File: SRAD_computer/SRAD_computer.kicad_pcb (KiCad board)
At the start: 2 copper layers, 80 x 90 mm, 73 parts, among them J1 Terminal_3, J2 Conn_01x02, J4 Terminal_2, J5 Connector_3_Pol, J6 Micro_SD_Card, J7 UJ20-C-H-G-SMT-6-P16-TR, Q1 MMBT5551L, Q3 FDN340P, U1 NCP1117-3.3_SOT223, U2 W25Q128JVS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

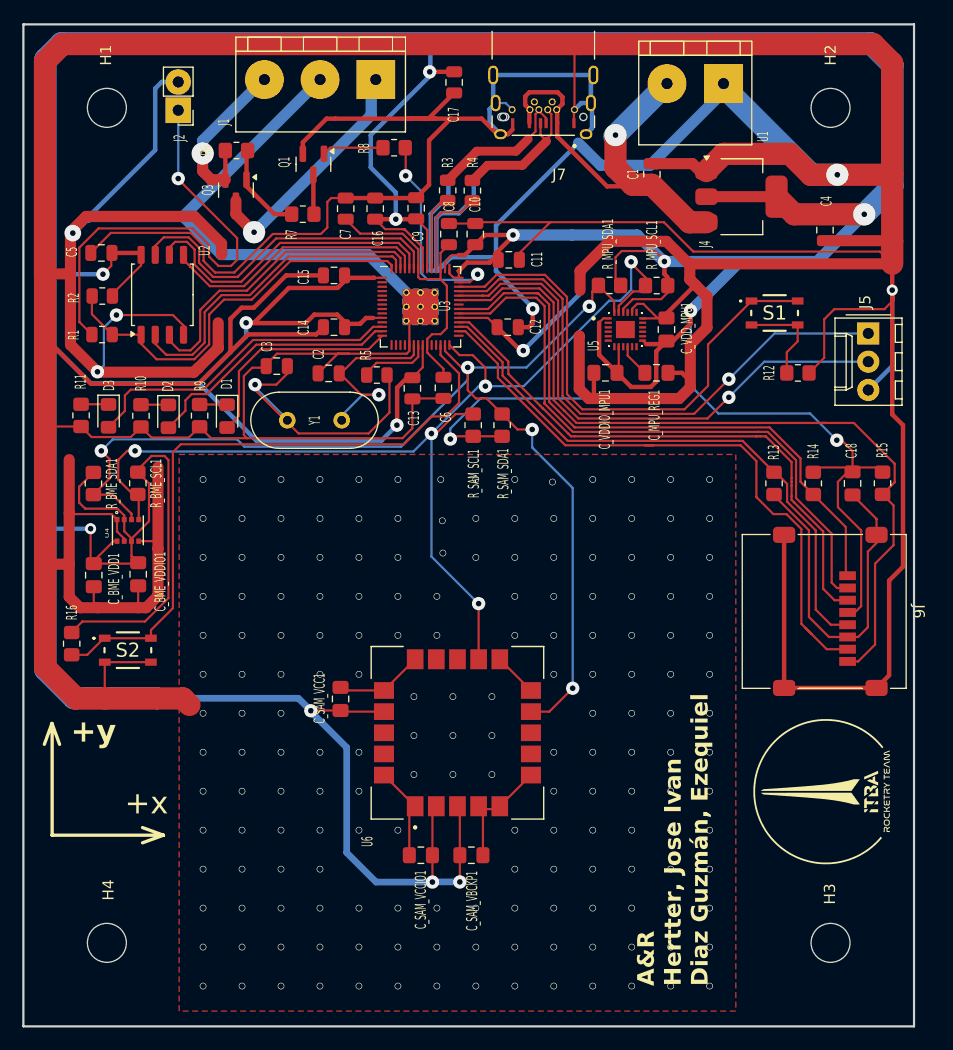
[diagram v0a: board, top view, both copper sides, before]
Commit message: reboot and bootsel buttons added
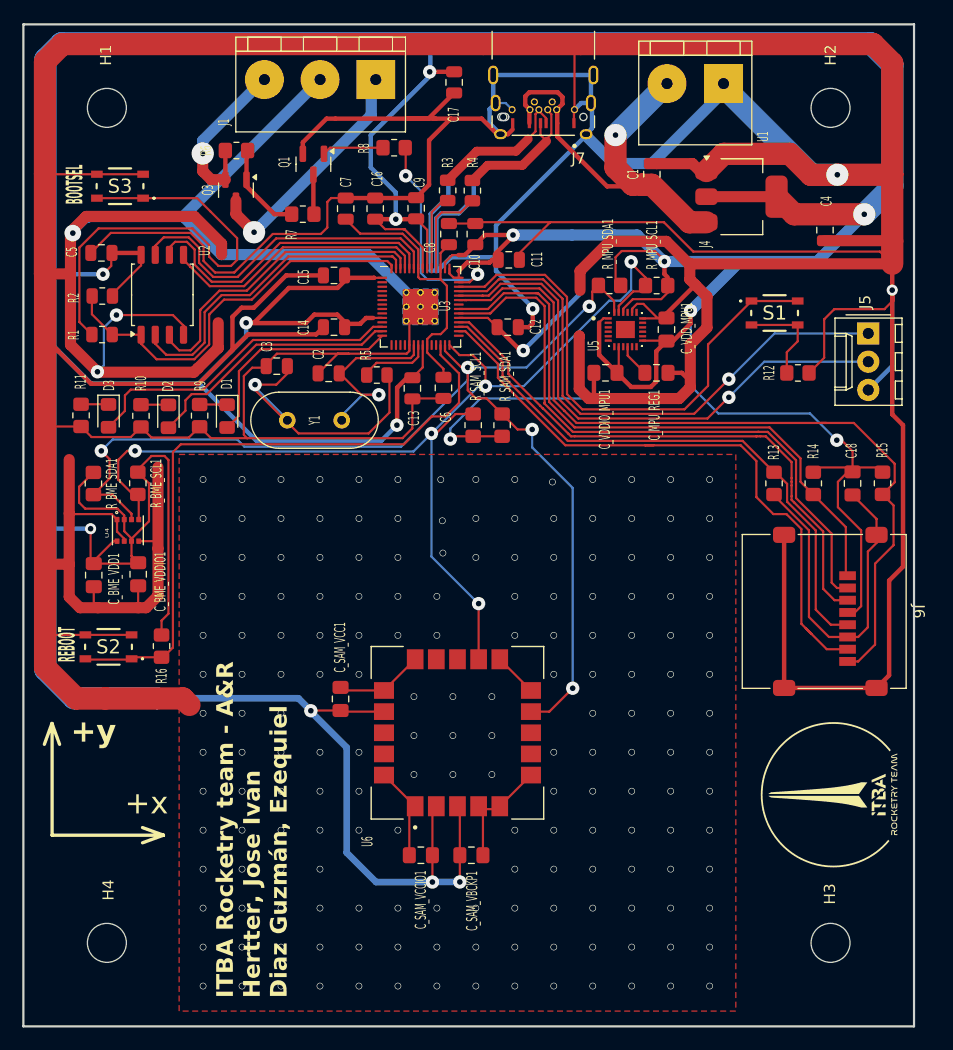
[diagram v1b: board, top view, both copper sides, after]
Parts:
- removed J2: Conn_01x02, Connector_PinHeader_2.54mm:PinHeader_1x02_P2.54mm_Vertical
- added S3: PTS810SJK250SMTR_LFS, Rocketry_FC:PTS810SJK250SMTRLFS, F.Cu at (64.6, 49.9)
- moved R16 8.07 mm to (68.3, 91.2)
- moved S2 1.77 mm to (63.5, 91.2), turned to 180 degrees
- moved G*** 0.73 mm to (128.8, 104.5)
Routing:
- net GND: track 951.9 -> 945.2 mm
- net +3V3: track 617.7 -> 611.1 mm
- net /~{USB_BOOT}: track 41.0 -> 41.4 mm, vias 1 -> 0
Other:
- board text added: "BOOTSEL"
- board text added: "ITBA Rocketry team - A&R Hertter, Jose Ivan Diaz Guzmán, Ezequiel"
- board text added: "REBOOT"
- board text removed: "A&R Hertter, Jose Ivan Diaz Guzmán, Ezequiel"

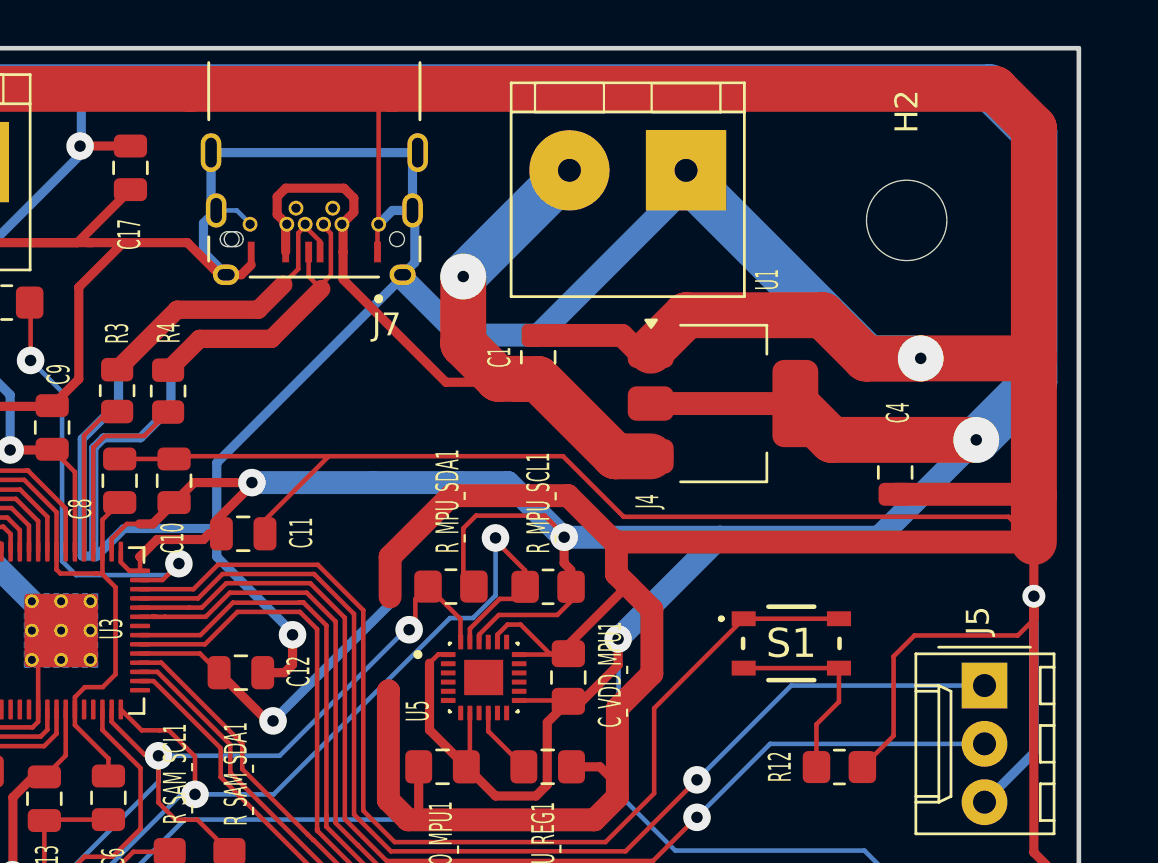
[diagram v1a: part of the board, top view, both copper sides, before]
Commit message: Pin for battery level added
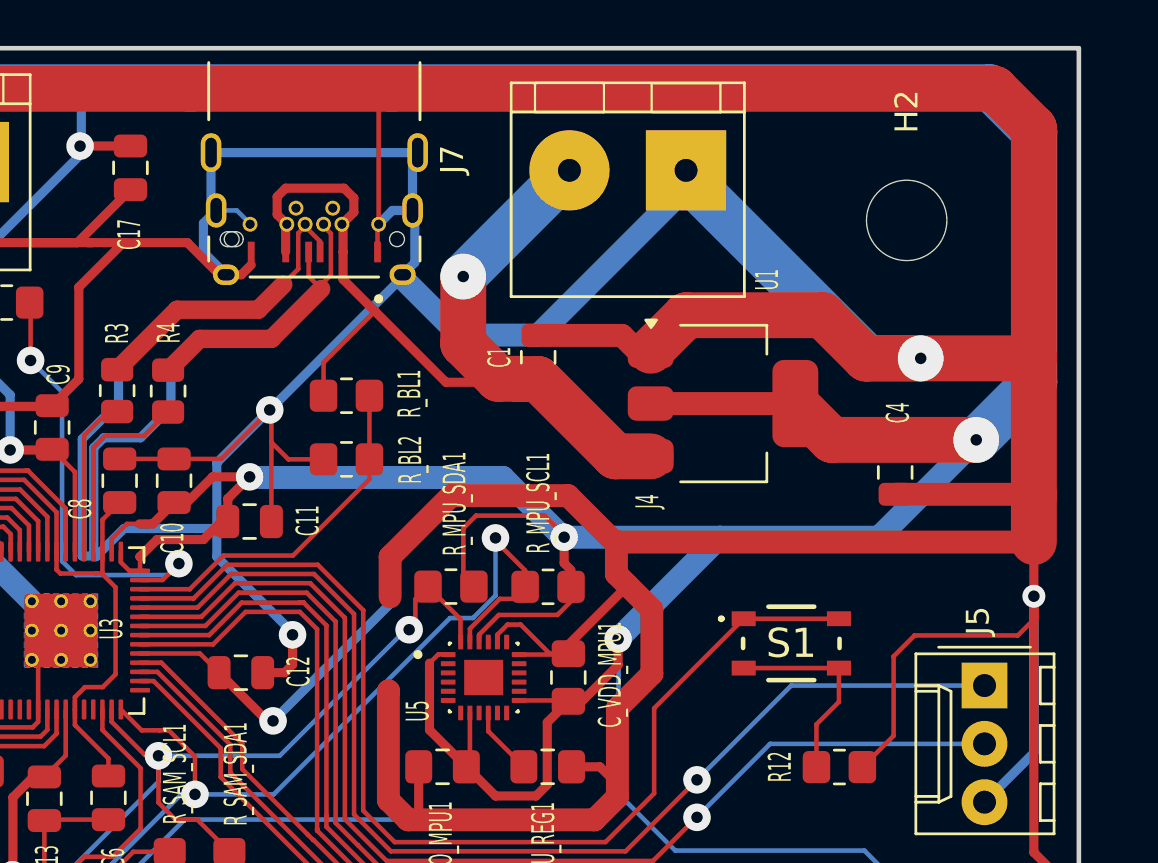
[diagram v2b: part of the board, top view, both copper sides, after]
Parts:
- added R_BL1: R, TCLib:R_0805, F.Cu at (104.0, 50.5)
- added R_BL2: R, TCLib:R_0805, F.Cu at (104.0, 53.2)
- moved C11 0.60 mm to (99.8, 55.9)
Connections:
- U3 pad 36: /GPIO24 -> /SD_DAT1
- U3 pad 37: /SD_DAT1 -> /UART_Tx
- U3 pad 38: /UART_Tx -> /UART_Rx
- U3 pad 39: /UART_Rx -> /SW_1
- U3 pad 40: /SW_1 -> /BAT_LVL
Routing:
- net GND: track 945.2 -> 914.6 mm, vias 184 -> 185
- net /BAT_LVL: track 0.00 -> 15.6 mm
- net VBUS: track 40.1 -> 44.7 mm
- net +3V3: track 611.1 -> 613.8 mm

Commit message: Gerber files added
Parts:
- removed Q1: MMBT5551L, Package_TO_SOT_SMD:SOT-23
- removed Q3: FDN340P, Package_TO_SOT_SMD:SOT-23
- removed R6, R7, R8: R, TCLib:R_0805
- J1: value Terminal_3 -> Connector_2_Pol; footprint TCLib:Bornera_3_P5mm -> TCLib:Molex_1x02_P2.54mm
- moved J1 1.69 mm to (85.8, 40.3), turned to 0 degrees
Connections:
- J1 pad 1: /V_cam -> GND
- J1 pad 2: GND -> /servo
- U3 pad 41: /power_cam -> /servo
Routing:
- net /servo: track 0.00 -> 26.5 mm, vias 0 -> 1
- net /V_cam: track 21.8 -> 0.00 mm, vias 1 -> 0
- net /power_cam: track 19.4 -> 0.00 mm, vias 2 -> 0
- net V_cam_bus: track 15.5 -> 0.00 mm, vias 1 -> 0
- net GND: track 914.6 -> 899.6 mm
- net Net-(Q3-G): track 8.35 -> 0.00 mm
- net Net-(Q1-B): track 5.53 -> 0.00 mm
- net Net-(Q1-C): track 3.57 -> 0.00 mm
- net +3V3: track 613.8 -> 611.9 mm

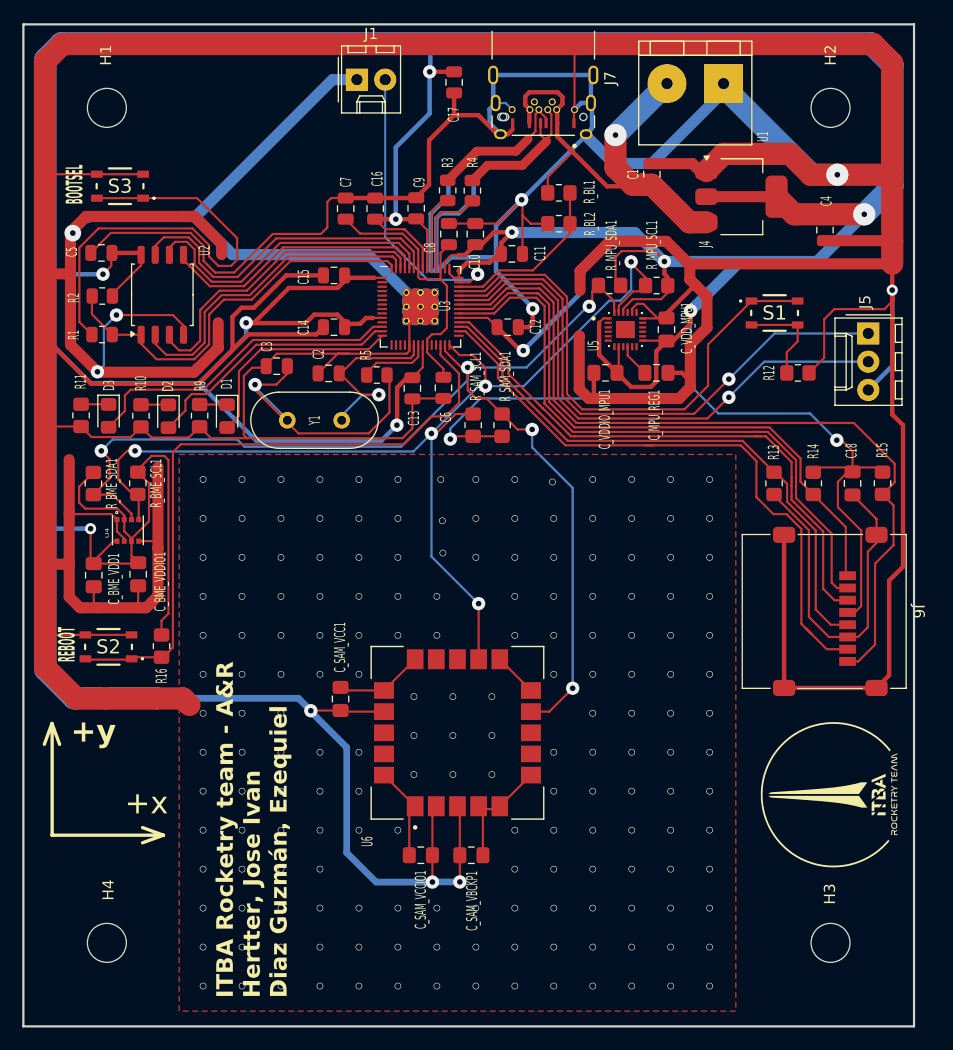
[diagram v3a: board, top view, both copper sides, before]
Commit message: changed SD socket & updated gerber files
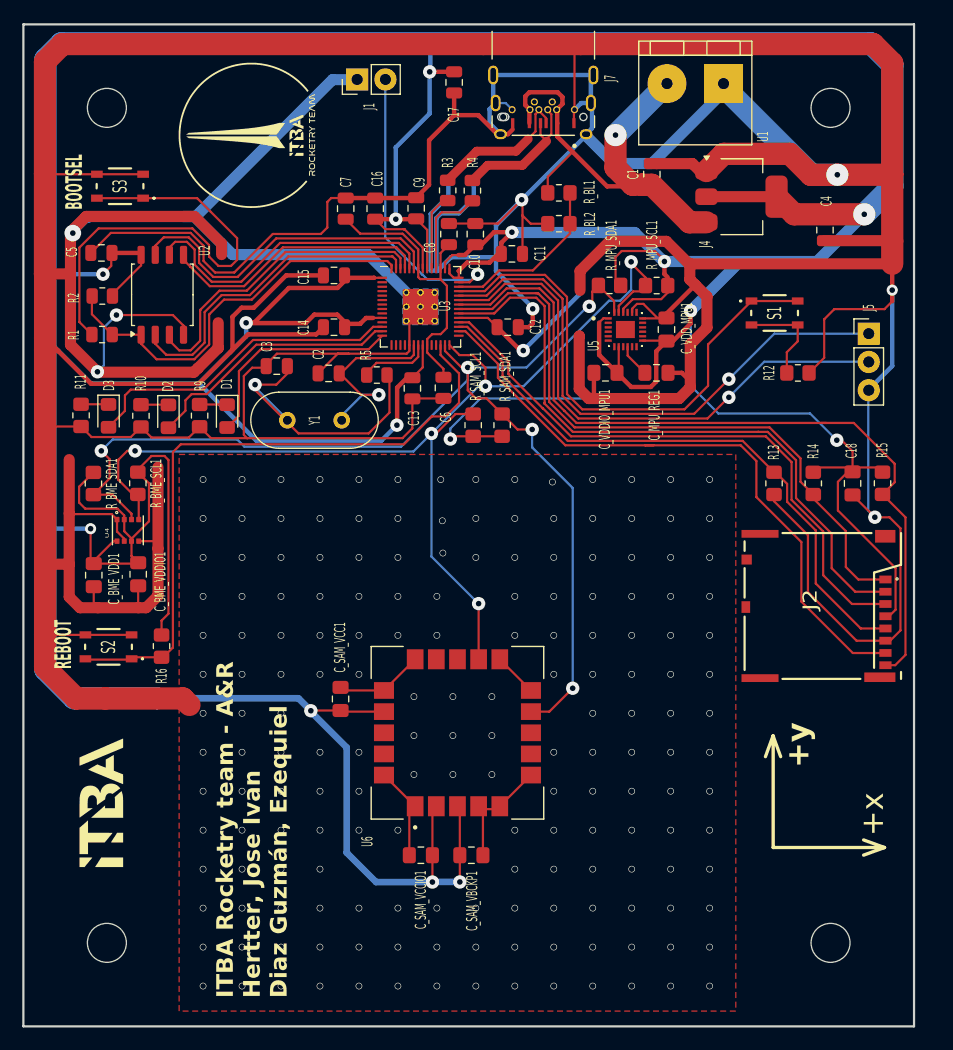
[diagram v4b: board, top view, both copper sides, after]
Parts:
- removed J6: Micro_SD_Card, my_lib:microSD_HC_Molex_47219-2001
- added G***: LOGO, my_lib:Logo_ITBA, F.Cu at (62.9, 105.2)
- added J2: 503398-1892, my_lib:503398-1892-1, F.Cu at (134.7, 81.0)
- J1: footprint TCLib:Molex_1x02_P2.54mm -> TCLib:PinHeader_1x02_P2.54mm_Vertical
- J5: footprint TCLib:Molex_1x03_P2.54mm -> TCLib:PinHeader_1x03_P2.54mm_Vertical
- S1, S2, S3: footprint Rocketry_FC:PTS810SJK250SMTRLFS -> my_lib:PTS810SJK250SMTRLFS
- moved G*** 79.0 mm to (76.5, 45.2)
- turned J5 to 0 degrees
- turned J1 to 90 degrees
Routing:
- net GND: track 899.6 -> 855.5 mm, vias 185 -> 186
- net /SD_DAT2: track 55.3 -> 58.4 mm
- net /SD_CMD: track 50.9 -> 53.7 mm
- net /SD_DAT3: track 56.8 -> 59.0 mm
- net /SD_CLK: track 51.8 -> 54.0 mm
- net +3V3: track 611.9 -> 613.2 mm
- net /SD_DAT0: track 55.9 -> 56.8 mm

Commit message: Rearranged some files
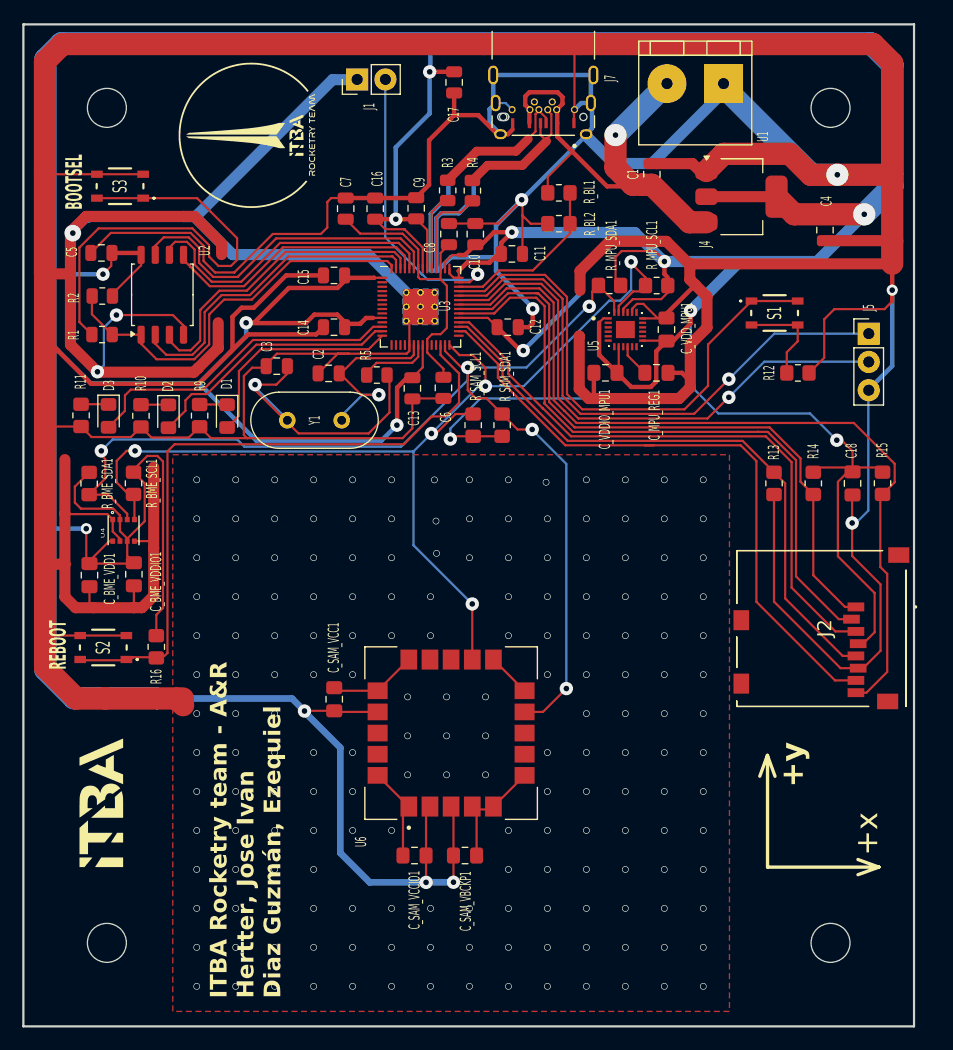
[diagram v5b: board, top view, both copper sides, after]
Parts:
- J2: footprint my_lib:503398-1892-1 -> my_lib:693071010811
- moved J2 11.2 mm to (127.6, 89.6), turned to 90 degrees
- moved C_SAM_VBCKP1 0.57 mm to (95.5, 110.0)
- moved U6 0.57 mm to (94.3, 99.0)
- moved C_SAM_VCC1 0.57 mm to (83.8, 95.9)
- moved C_SAM_VCCIO1 0.57 mm to (91.0, 110.0)
- moved R16 0.47 mm to (67.8, 91.2)
- moved S2 0.47 mm to (63.1, 91.3)
- moved U4 0.39 mm to (64.9, 80.8)
- moved C_BME_VDD1 0.39 mm to (61.8, 84.8)
- moved R_BME_SDA1 0.39 mm to (61.8, 76.6)
- moved C_BME_VDDIO1 0.39 mm to (65.8, 84.7)
- moved R_BME_SCL1 0.39 mm to (65.8, 76.5)
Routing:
- net GND: track 855.5 -> 858.7 mm
- net /SD_DAT1: track 72.6 -> 75.0 mm
- net +3V3: track 613.2 -> 615.1 mm
- net /SD_DAT0: track 56.8 -> 57.6 mm
- net /SD_CLK: track 54.0 -> 54.7 mm
- net /SD_CMD: track 53.7 -> 54.4 mm
- net /SD_DAT2: track 58.4 -> 58.9 mm

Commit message: Changed micro SD socket footprint
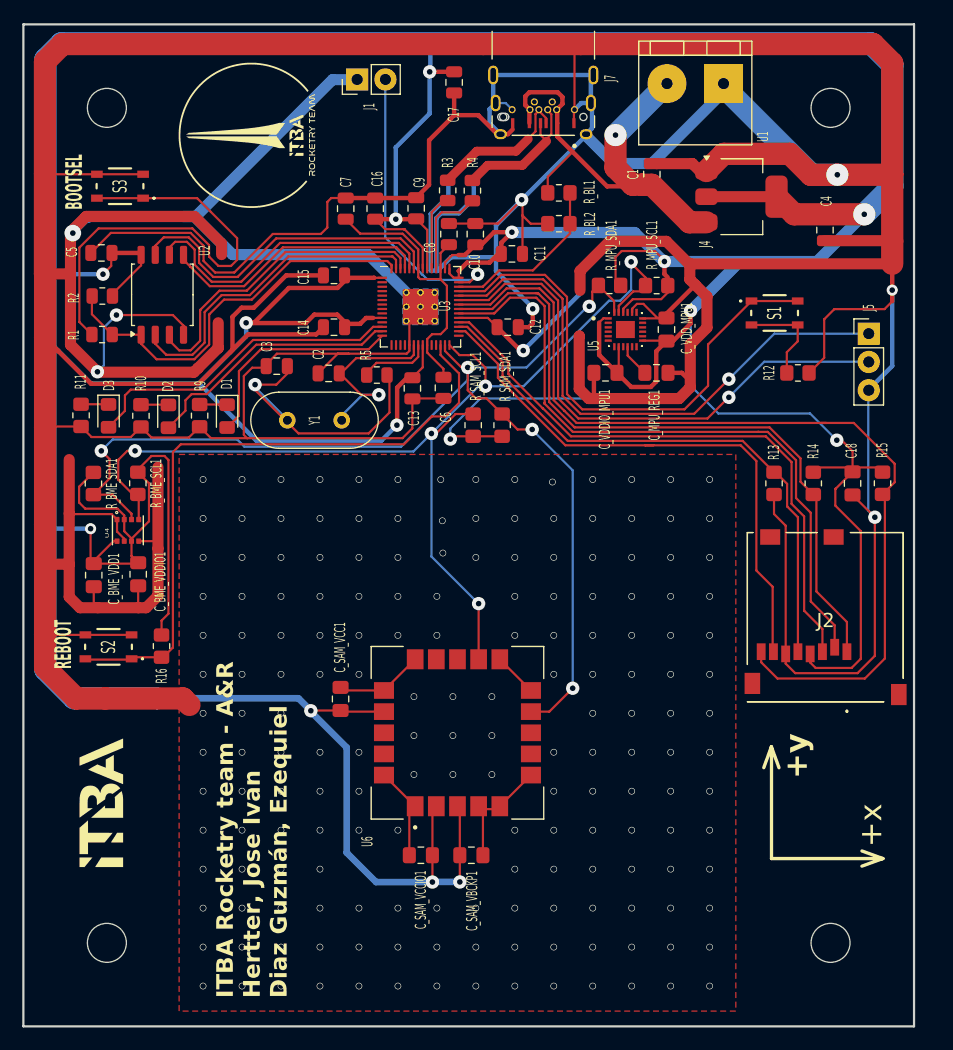
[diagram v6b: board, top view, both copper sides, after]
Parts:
- moved J2 1.08 mm to (127.9, 88.6), turned to 0 degrees
- moved C_SAM_VBCKP1 0.57 mm to (96.1, 110.0)
- moved U6 0.57 mm to (94.9, 99.0)
- moved C_SAM_VCC1 0.57 mm to (84.4, 95.9)
- moved C_SAM_VCCIO1 0.57 mm to (91.6, 110.0)
- moved R16 0.47 mm to (68.3, 91.2)
- moved S2 0.47 mm to (63.5, 91.2)
- moved U4 0.39 mm to (65.3, 80.8)
- moved C_BME_VDD1 0.39 mm to (62.2, 84.8)
- moved R_BME_SDA1 0.39 mm to (62.2, 76.6)
- moved C_BME_VDDIO1 0.39 mm to (66.2, 84.7)
- moved R_BME_SCL1 0.39 mm to (66.2, 76.5)
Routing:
- net /SD_DAT1: track 75.0 -> 83.3 mm
- net /SD_DAT0: track 57.6 -> 50.6 mm
- net +3V3: track 615.1 -> 621.0 mm
- net /SD_DAT2: track 58.9 -> 62.4 mm
- net /SD_CLK: track 54.7 -> 51.5 mm
- net GND: track 858.7 -> 860.2 mm
- net /SD_DAT3: track 59.2 -> 60.5 mm
- net /SD_CMD: track 54.4 -> 53.9 mm
